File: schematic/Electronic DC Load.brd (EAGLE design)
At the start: 100 x 51.5 mm, 104 parts, among them J1 POWER_JACKPTH_LOCK, J2 AVR_SPI_PROG_3X2PTH, J3 FAN, J4 KF762-2, Q1 16MHz, Q2 IRFP250NV, Q3 600mA/40V, U1 AMS1117-5.0, U10 AD8629ARZ, U2 REF5050_D_8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

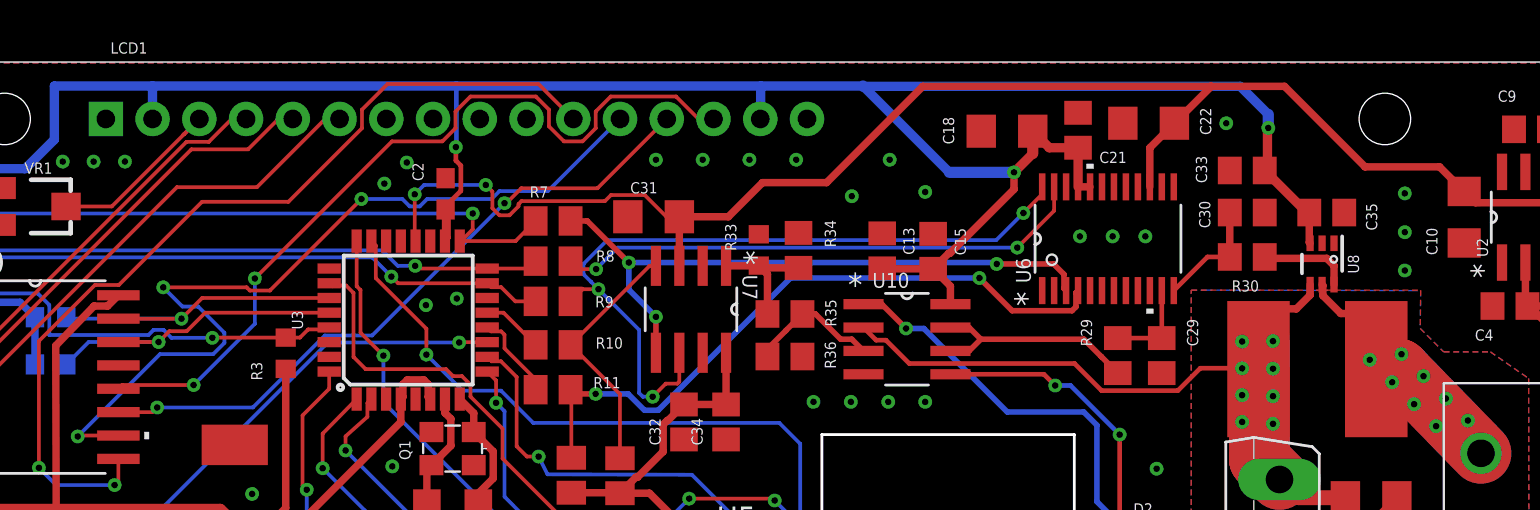
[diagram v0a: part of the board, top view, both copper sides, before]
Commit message: Make the ground connection of Rsense a litte stronger
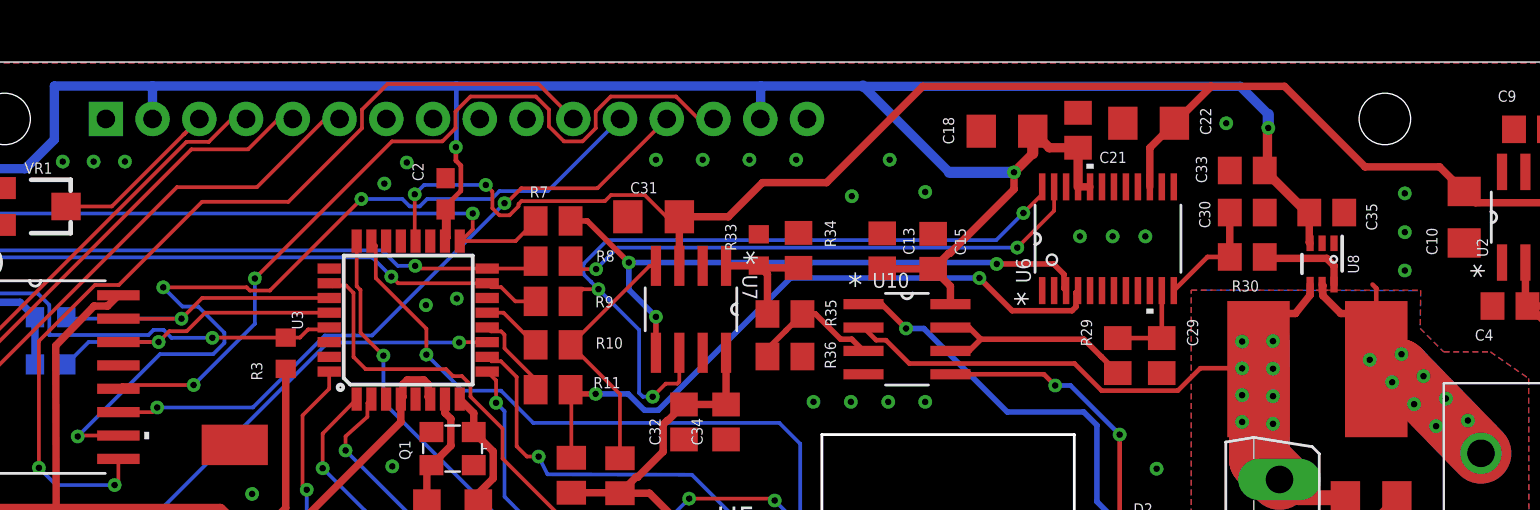
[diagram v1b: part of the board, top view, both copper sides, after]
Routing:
- net GND: track 22.0 -> 26.6 mm
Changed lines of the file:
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@@
 <setting verticaltext="up"/>
 </settings>
-<grid distance="50" unitdist="mil" unit="mm" style="lines" multiple="1" display="no" altdistance="1" altunitdist="mil" altunit="mil"/>
+<grid distance="50" unitdist="mil" unit="mil" style="lines" multiple="1" display="no" altdistance="1" altunitdist="mil" altunit="mil"/>
 <layers>
 <layer number="1" name="Top" color="4" fill="1" visible="yes" active="yes"/>
@@
 </element>
 <element name="LCD1" library="SparkFun-Displays" package="LCD-16X2_NOSILK" value="LCD-16X2NOSILK" x="46.99" y="32.8676" smashed="yes">
-<attribute name="NAME" x="15.24" y="51.9176" size="0.6096" layer="25" font="vector" ratio="20"/>
 <attribute name="SF_ID" value="LCD-00255" x="46.99" y="32.8676" size="1.778" layer="27" display="off"/>
 <attribute name="VALUE" x="15.24" y="13.8176" size="0.6096" layer="27" font="vector" ratio="20" align="top-left"/>
@@
 </polygon>
 <wire x1="89.7128" y1="30.2006" x2="85.2678" y2="34.7726" width="3.302" layer="1"/>
-<wire x1="84.0228" y1="34.7726" x2="85.2678" y2="34.7726" width="3.302" layer="1"/>
+<wire x1="85.2678" y1="34.7726" x2="84.0228" y2="34.7726" width="3.302" layer="1"/>
 <wire x1="89.7128" y1="30.2006" x2="85.344" y2="34.6964" width="3.302" layer="16"/>
 <wire x1="85.344" y1="34.6964" x2="84.1502" y2="34.6964" width="3.302" layer="16"/>
@@
 <via x="22.6314" y="11.176" extent="1-16" drill="0.35"/>
 <via x="23.7744" y="11.2014" extent="1-16" drill="0.35"/>
+<wire x1="84.0228" y1="34.7726" x2="84.0228" y2="39.1672" width="0.254" layer="1"/>
+<wire x1="84.0228" y1="39.1672" x2="83.82" y2="39.37" width="0.254" layer="1"/>
 </signal>
 <signal name="N$11">
@@
 <wire x1="79.8068" y1="27.7876" x2="82.3438" y2="27.7876" width="0.8128" layer="1"/>
 <wire x1="80.4268" y1="39.3626" x2="80.4268" y2="38.7962" width="0.4064" layer="1"/>
-<wire x1="80.4268" y1="38.7962" x2="79.6798" y2="38.0492" width="0.4064" layer="1"/>
-<wire x1="79.6798" y1="38.0492" x2="78.0288" y2="38.0492" width="0.4064" layer="1"/>
-<wire x1="77.8764" y1="37.8968" x2="78.0288" y2="38.0492" width="0.4064" layer="1"/>
+<wire x1="80.4268" y1="38.7962" x2="79.629" y2="37.7952" width="0.4064" layer="1"/>
+<wire x1="79.629" y1="37.7952" x2="77.978" y2="37.7952" width="0.4064" layer="1"/>
+<wire x1="77.8764" y1="37.8968" x2="77.978" y2="37.7952" width="0.4064" layer="1"/>
 <wire x1="77.8764" y1="37.8968" x2="77.724" y2="37.7444" width="0.4064" layer="1"/>
 <wire x1="77.6734" y1="34.8232" x2="77.6228" y2="34.7726" width="0.4064" layer="1"/>
